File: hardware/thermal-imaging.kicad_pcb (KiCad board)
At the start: 2 copper layers, 40 x 40 mm, 48 parts, among them P1 CON-SENSOR, P2 Boot, P3 Debug, Q1 25MHz, U1 XMC1302-32, U10 DRILL, U11 DRILL, U2 74LVC1G17, U3 74LVC1G17, U4 FLIR-Lepton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

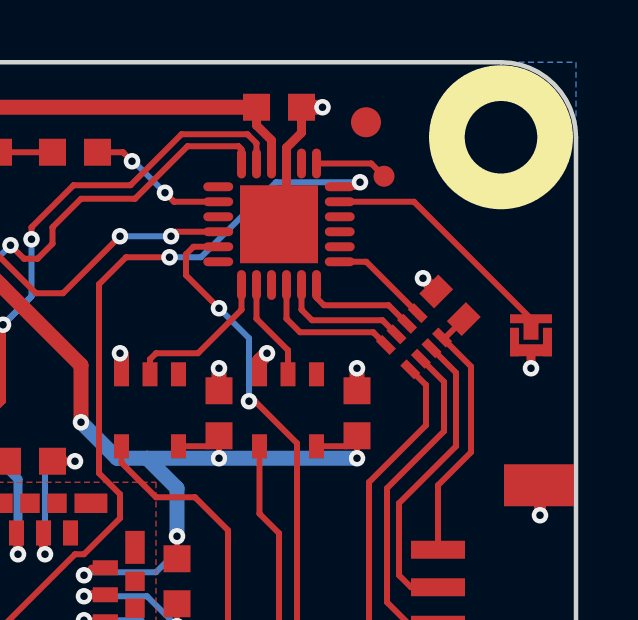
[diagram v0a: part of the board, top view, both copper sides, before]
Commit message: Change capacitor footprint(s) to C0402F
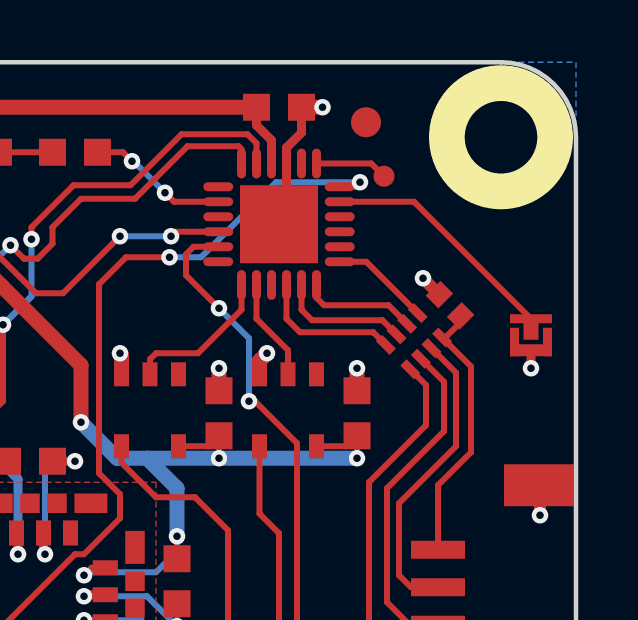
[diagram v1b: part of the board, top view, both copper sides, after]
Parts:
- C16: footprint kicad-libraries:C0402E -> kicad-libraries:C0402F
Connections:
- P1 pad 1: (no net) -> Net-(P1-Pad1)
- RP2 pad 6: (no net) -> Net-(RP2-Pad6)
- RP2 pad 7: (no net) -> Net-(RP2-Pad7)
- RP3 pad 4: (no net) -> Net-(RP3-Pad4)
- RP3 pad 5: (no net) -> Net-(RP3-Pad5)
- U1 pad 13: (no net) -> Net-(U1-Pad13)
- U1 pad 15: (no net) -> Net-(U1-Pad15)
- U1 pad 18: (no net) -> Net-(U1-Pad18)
- U1 pad 2: (no net) -> Net-(U1-Pad2)
- U1 pad 21: (no net) -> Net-(U1-Pad21)
- U1 pad 3: (no net) -> Net-(U1-Pad3)
- U1 pad 4: (no net) -> Net-(U1-Pad4)
- U1 pad 8: (no net) -> Net-(U1-Pad8)
- U4 pad 17: (no net) -> Net-(U4-Pad17)
- U4 pad 28: (no net) -> Net-(U4-Pad28)
- U4 pad 29: (no net) -> Net-(U4-Pad29)
- U4 pad 3: (no net) -> Net-(U4-Pad3)
- U4 pad 31: (no net) -> Net-(U4-Pad31)
- U4 pad 32: (no net) -> Net-(U4-Pad32)
- U4 pad 4: (no net) -> Net-(U4-Pad4)
- U4 pad 5: (no net) -> Net-(U4-Pad5)
